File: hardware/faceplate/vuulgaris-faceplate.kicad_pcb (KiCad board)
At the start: 4 copper layers, 298.3 x 137.8 mm, 54 parts, among them J1 HX JN2.54-2x5P TP H8.9, U1 MSP430FR2675TPT, Y1 32.768kHz FC-135 12.5pF

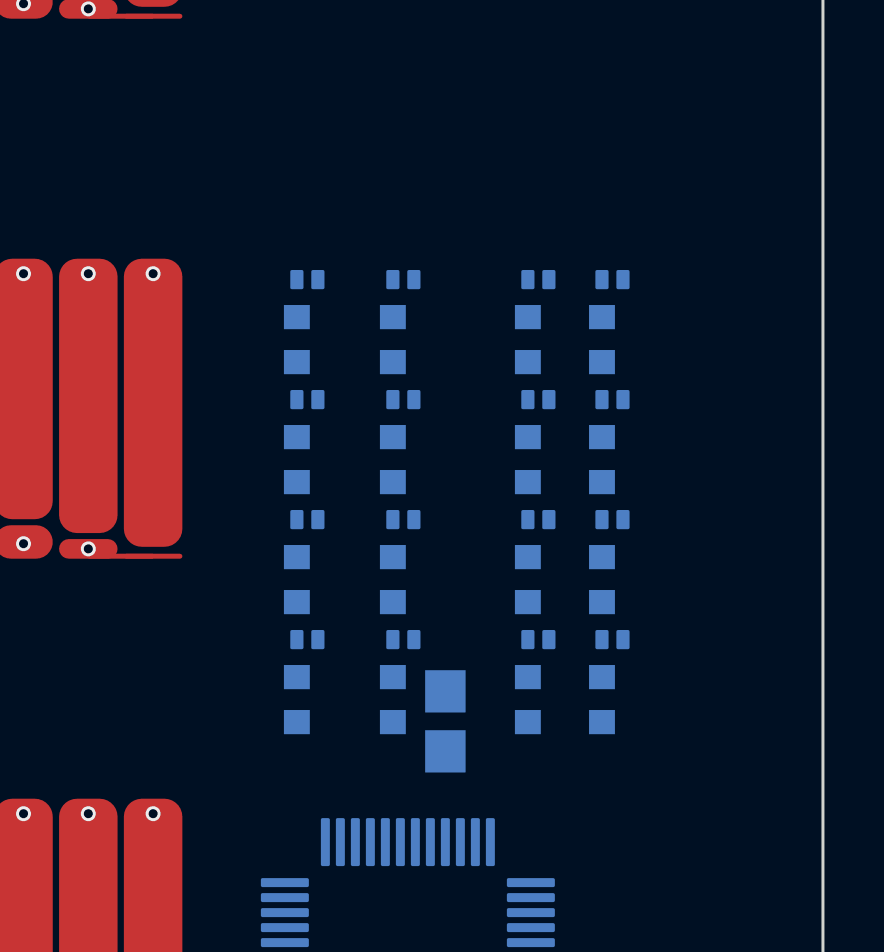
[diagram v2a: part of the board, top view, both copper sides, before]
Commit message: faceplate: open the network grid for routing; CapTIvate netclass
Dylan asked whether the grid had room to route. Measured at the board's
rules (0.25 / 0.2, so three traces need 1.55mm), not everywhere: RX3's
channel was 1.12mm past the TVS rows -- the price of pulling it off the
wall -- and there was nowhere for the lines to come up from L2: at 4mm
row pitch a TVS sat 0.5mm under the R above it.

- Rows 4.0 -> 5.0mm apart, growing upward into empty margin; row 4 and
  the fan-out into U1 are unchanged. Every cell now has a via spot on
  its column line, 2.9 above the R's centre, touching no channel.
- Columns 0-2 back 0.45 (C3 with them): RX3's channel 1.57mm; the left
  channel Dylan widened keeps 2.73.
- Netclass CapTIvate for /PAD* and /CAP*: 0.15 track, 0.15 clearance,
  0.5/0.3 vias. Thin sensor traces are what TI wants anyway.
- boardcheck matched netclass patterns by exact name only, so wildcard
  classes silently got Default; it now matches them as KiCad does. The
  main board's patterns are all exact names, unaffected.

Proven on a scratch copy: all 16 vias placed and three 0.15 traces down
RX3's channel and past C3 -- DRC and boardcheck clean; a trace planted
0.06mm off R34's pad fails with 7 clearance errors. Re-placed against
the previous commit, only the grid and C3 moved.

Checked: mksch/netcheck 145/145; boardcheck parity 0, clearance 0; DRC
--unrouted 0 errors; panelcheck --strict 13 OK.
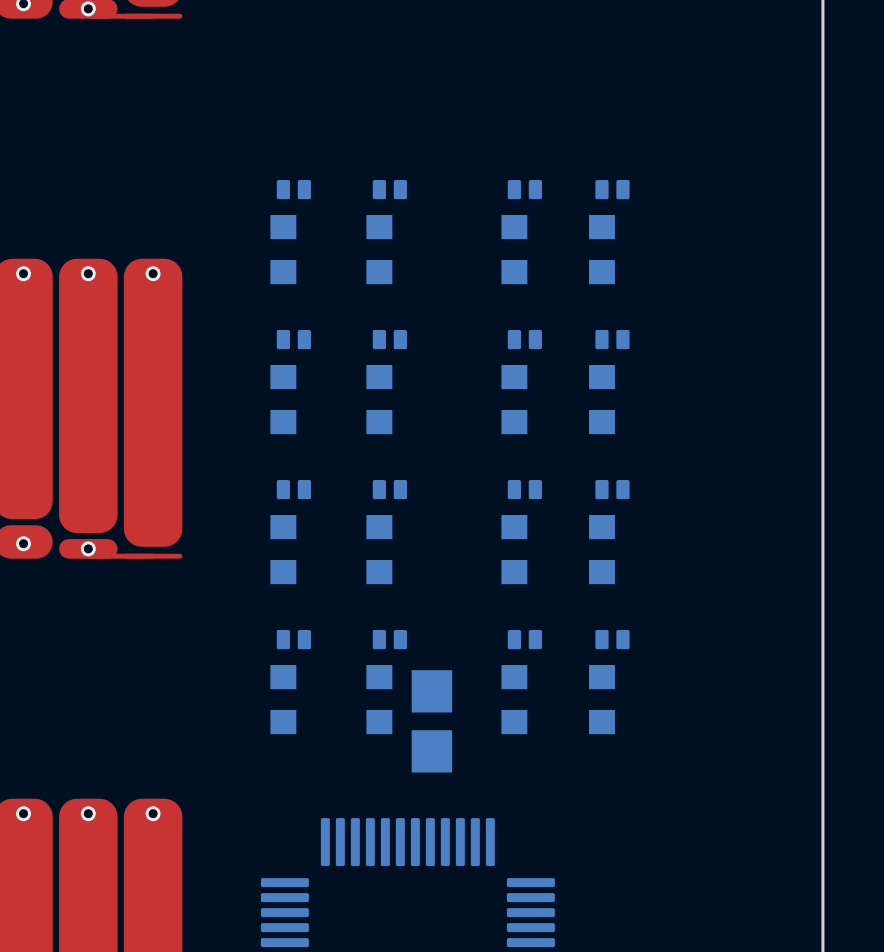
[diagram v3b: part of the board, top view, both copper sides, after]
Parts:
- moved D11 3.03 mm to (380.6, 128.2)
- moved D12 3.03 mm to (383.9, 128.2)
- moved D13 3.03 mm to (388.4, 128.2)
- moved R11 3.03 mm to (380.3, 130.2)
- moved R12 3.03 mm to (383.5, 130.2)
- moved R13 3.03 mm to (388.0, 130.2)
- moved D14 3.00 mm to (391.3, 128.2)
- moved R14 3.00 mm to (390.9, 130.2)
- moved D21 2.05 mm to (380.6, 133.2)
- moved D22 2.05 mm to (383.9, 133.2)
- moved D23 2.05 mm to (388.4, 133.2)
- moved R21 2.05 mm to (380.3, 135.2)
- moved R22 2.05 mm to (383.5, 135.2)
- moved R23 2.05 mm to (388.0, 135.2)
- moved D24 2.00 mm to (391.3, 133.2)
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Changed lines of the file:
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@@
   )
   (footprint "vuulgaris:R0603" (layer "B.Cu")
-    (at 383.95 145.15 -90)
+    (at 383.5 145.15 -90)
     (property "Sheetfile" "vuulgaris-faceplate.kicad_sch")
     (property "Sheetname" "")
@@
   )
   (footprint "vuulgaris:X1SON-2_DPY0002A" (layer "B.Cu")
-    (at 388.8 143.15)
+    (at 388.35 143.15)
     (descr "TI DPY0002A X1SON-2 (0402), TPD1E10B06DPYR. TI land pattern 4224561/C: openings 0.3 x 0.5, centres 0.7, solder-mask-defined (TI preferred), copper 0.07 under mask")
     (tags "X1SON DPY0002A TPD1E10B06 0402 TVS")
@@
   )
   (footprint "vuulgaris:R0603" (layer "B.Cu")
-    (at 390.92 137.15 -90)
+    (at 390.92 135.15 -90)
     (property "Sheetfile" "vuulgaris-faceplate.kicad_sch")
     (property "Sheetname" "")
@@
   )
   (footprint "vuulgaris:R0603" (layer "B.Cu")
-    (at 383.95 137.15 -90)
+    (at 383.5 135.15 -90)
     (property "Sheetfile" "vuulgaris-faceplate.kicad_sch")
     (property "Sheetname" "")
@@
   )
   (footprint "vuulgaris:X1SON-2_DPY0002A" (layer "B.Cu")
-    (at 384.3 131.15)
+    (at 383.85 128.15)
     (descr "TI DPY0002A X1SON-2 (0402), TPD1E10B06DPYR. TI land pattern 4224561/C: openings 0.3 x 0.5, centres 0.7, solder-mask-defined (TI preferred), copper 0.07 under mask")
     (tags "X1SON DPY0002A TPD1E10B06 0402 TVS")
@@
   )
   (footprint "vuulgaris:R0603" (layer "B.Cu")
-    (at 388.45 137.15 -90)
+    (at 388 135.15 -90)
     (property "Sheetfile" "vuulgaris-faceplate.kicad_sch")
     (property "Sheetname" "")
@@
   )
   (footprint "vuulgaris:R0603" (layer "B.Cu")
-    (at 388.45 141.15 -90)
+    (at 388 140.15 -90)
     (property "Sheetfile" "vuulgaris-faceplate.kicad_sch")
     (property "Sheetname" "")
@@
   )
   (footprint "vuulgaris:R0603" (layer "B.Cu")
-    (at 383.95 141.15 -90)
+    (at 383.5 140.15 -90)
     (property "Sheetfile" "vuulgaris-faceplate.kicad_sch")
     (property "Sheetname" "")
@@
   )
   (footprint "vuulgaris:X1SON-2_DPY0002A" (layer "B.Cu")
-    (at 381.1 135.15)
+    (at 380.65 133.15)
     (descr "TI DPY0002A X1SON-2 (0402), TPD1E10B06DPYR. TI land pattern 4224561/C: openings 0.3 x 0.5, centres 0.7, solder-mask-defined (TI preferred), copper 0.07 under mask")
     (tags "X1SON DPY0002A TPD1E10B06 0402 TVS")
@@
   )
   (footprint "vuulgaris:X1SON-2_DPY0002A" (layer "B.Cu")
-    (at 391.27 135.15)
+    (at 391.27 133.15)
     (descr "TI DPY0002A X1SON-2 (0402), TPD1E10B06DPYR. TI land pattern 4224561/C: openings 0.3 x 0.5, centres 0.7, solder-mask-defined (TI preferred), copper 0.07 under mask")
     (tags "X1SON DPY0002A TPD1E10B06 0402 TVS")
@@
   )
   (footprint "vuulgaris:R0603" (layer "B.Cu")
-    (at 390.92 141.15 -90)
+    (at 390.92 140.15 -90)
     (property "Sheetfile" "vuulgaris-faceplate.kicad_sch")
     (property "Sheetname" "")
@@
   )
   (footprint "vuulgaris:X1SON-2_DPY0002A" (layer "B.Cu")
-    (at 381.1 139.15)
+    (at 380.65 138.15)
     (descr "TI DPY0002A X1SON-2 (0402), TPD1E10B06DPYR. TI land pattern 4224561/C: openings 0.3 x 0.5, centres 0.7, solder-mask-defined (TI preferred), copper 0.07 under mask")
     (tags "X1SON DPY0002A TPD1E10B06 0402 TVS")
@@
   )
   (footprint "vuulgaris:X1SON-2_DPY0002A" (layer "B.Cu")
-    (at 388.8 139.15)
+    (at 388.35 138.15)
     (descr "TI DPY0002A X1SON-2 (0402), TPD1E10B06DPYR. TI land pattern 4224561/C: openings 0.3 x 0.5, centres 0.7, solder-mask-defined (TI preferred), copper 0.07 under mask")
     (tags "X1SON DPY0002A TPD1E10B06 0402 TVS")
@@
   )
   (footprint "vuulgaris:X1SON-2_DPY0002A" (layer "B.Cu")
-    (at 384.3 139.15)
+    (at 383.85 138.15)
     (descr "TI DPY0002A X1SON-2 (0402), TPD1E10B06DPYR. TI land pattern 4224561/C: openings 0.3 x 0.5, centres 0.7, solder-mask-defined (TI preferred), copper 0.07 under mask")
     (tags "X1SON DPY0002A TPD1E10B06 0402 TVS")
@@
   )
   (footprint "vuulgaris:C0805" (layer "B.Cu")
-    (at 385.7 145.875 90)
+    (at 385.25 145.875 90)
     (descr "10uF (106) ±10% 25V")
     (property "Sheetfile" "vuulgaris-faceplate.kicad_sch")
@@
     (property "ki_keywords" "cap capacitor")
     (attr smd)
-    (fp_text reference "C3" (at 2.9 0 180) (layer "B.SilkS")
+    (fp_text reference "C3" (at 3.275 0 180) (layer "B.SilkS")
         (effects (font (size 0.8 0.8) (thickness 0.12)) (justify mirror))
     )
@@
   )
   (footprint "vuulgaris:R0603" (layer "B.Cu")
-    (at 380.75 137.15 -90)
+    (at 380.3 135.15 -90)
     (property "Sheetfile" "vuulgaris-faceplate.kicad_sch")
     (property "Sheetname" "")
@@
   )
   (footprint "vuulgaris:R0603" (layer "B.Cu")
-    (at 380.75 141.15 -90)
+    (at 380.3 140.15 -90)
     (property "Sheetfile" "vuulgaris-faceplate.kicad_sch")
     (property "Sheetname" "")
@@
   )
   (footprint "vuulgaris:X1SON-2_DPY0002A" (layer "B.Cu")
-    (at 384.3 143.15)
+    (at 383.85 143.15)
     (descr "TI DPY0002A X1SON-2 (0402), TPD1E10B06DPYR. TI land pattern 4224561/C: openings 0.3 x 0.5, centres 0.7, solder-mask-defined (TI preferred), copper 0.07 under mask")
     (tags "X1SON DPY0002A TPD1E10B06 0402 TVS")
@@
   )
   (footprint "vuulgaris:X1SON-2_DPY0002A" (layer "B.Cu")
-    (at 381.1 131.15)
+    (at 380.65 128.15)
     (descr "TI DPY0002A X1SON-2 (0402), TPD1E10B06DPYR. TI land pattern 4224561/C: openings 0.3 x 0.5, centres 0.7, solder-mask-defined (TI preferred), copper 0.07 under mask")
     (tags "X1SON DPY0002A TPD1E10B06 0402 TVS")
@@
   )
   (footprint "vuulgaris:R0603" (layer "B.Cu")
-    (at 390.92 133.15 -90)
+    (at 390.92 130.15 -90)
     (property "Sheetfile" "vuulgaris-faceplate.kicad_sch")
     (property "Sheetname" "")
@@
   )
   (footprint "vuulgaris:X1SON-2_DPY0002A" (layer "B.Cu")
-    (at 381.1 143.15)
+    (at 380.65 143.15)
     (descr "TI DPY0002A X1SON-2 (0402), TPD1E10B06DPYR. TI land pattern 4224561/C: openings 0.3 x 0.5, centres 0.7, solder-mask-defined (TI preferred), copper 0.07 under mask")
     (tags "X1SON DPY0002A TPD1E10B06 0402 TVS")
@@
   )
   (footprint "vuulgaris:R0603" (layer "B.Cu")
-    (at 388.45 145.15 -90)
+    (at 388 145.15 -90)
     (property "Sheetfile" "vuulgaris-faceplate.kicad_sch")
     (property "Sheetname" "")
@@
   )
   (footprint "vuulgaris:X1SON-2_DPY0002A" (layer "B.Cu")
-    (at 391.27 139.15)
+    (at 391.27 138.15)
     (descr "TI DPY0002A X1SON-2 (0402), TPD1E10B06DPYR. TI land pattern 4224561/C: openings 0.3 x 0.5, centres 0.7, solder-mask-defined (TI preferred), copper 0.07 under mask")
     (tags "X1SON DPY0002A TPD1E10B06 0402 TVS")
@@
   )
   (footprint "vuulgaris:X1SON-2_DPY0002A" (layer "B.Cu")
-    (at 384.3 135.15)
+    (at 383.85 133.15)
     (descr "TI DPY0002A X1SON-2 (0402), TPD1E10B06DPYR. TI land pattern 4224561/C: openings 0.3 x 0.5, centres 0.7, solder-mask-defined (TI preferred), copper 0.07 under mask")
     (tags "X1SON DPY0002A TPD1E10B06 0402 TVS")
@@
   )
   (footprint "vuulgaris:R0603" (layer "B.Cu")
-    (at 380.75 133.15 -90)
+    (at 380.3 130.15 -90)
     (property "Sheetfile" "vuulgaris-faceplate.kicad_sch")
     (property "Sheetname" "")
@@
   )
   (footprint "vuulgaris:X1SON-2_DPY0002A" (layer "B.Cu")
-    (at 391.27 131.15)
+    (at 391.27 128.15)
     (descr "TI DPY0002A X1SON-2 (0402), TPD1E10B06DPYR. TI land pattern 4224561/C: openings 0.3 x 0.5, centres 0.7, solder-mask-defined (TI preferred), copper 0.07 under mask")
     (tags "X1SON DPY0002A TPD1E10B06 0402 TVS")
@@
   )
   (footprint "vuulgaris:R0603" (layer "B.Cu")
-    (at 388.45 133.15 -90)
+    (at 388 130.15 -90)
     (property "Sheetfile" "vuulgaris-faceplate.kicad_sch")
     (property "Sheetname" "")
@@
   )
   (footprint "vuulgaris:R0603" (layer "B.Cu")
-    (at 383.95 133.15 -90)
+    (at 383.5 130.15 -90)
     (property "Sheetfile" "vuulgaris-faceplate.kicad_sch")
     (property "Sheetname" "")
@@
   )
   (footprint "vuulgaris:X1SON-2_DPY0002A" (layer "B.Cu")
-    (at 388.8 135.15)
+    (at 388.35 133.15)
     (descr "TI DPY0002A X1SON-2 (0402), TPD1E10B06DPYR. TI land pattern 4224561/C: openings 0.3 x 0.5, centres 0.7, solder-mask-defined (TI preferred), copper 0.07 under mask")
     (tags "X1SON DPY0002A TPD1E10B06 0402 TVS")
@@
   )
   (footprint "vuulgaris:X1SON-2_DPY0002A" (layer "B.Cu")
-    (at 388.8 131.15)
+    (at 388.35 128.15)
     (descr "TI DPY0002A X1SON-2 (0402), TPD1E10B06DPYR. TI land pattern 4224561/C: openings 0.3 x 0.5, centres 0.7, solder-mask-defined (TI preferred), copper 0.07 under mask")
     (tags "X1SON DPY0002A TPD1E10B06 0402 TVS")
@@
   )
   (footprint "vuulgaris:R0603" (layer "B.Cu")
-    (at 380.75 145.15 -90)
-    (property "Sheetfile" "vuulgaris-faceplate.kicad_sch")
-    (property "Sheetname" "")
+    (at 380.3 145.15 -90)
+    (property "Sheetfile" "vuulgaris-faceplate.kicad_sch")
+    (property "Sheetname" "")
